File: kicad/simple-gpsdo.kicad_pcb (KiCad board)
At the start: 2 copper layers, 119.5 x 74.5 mm, 90 parts, among them J1 PPS_OUT, J2 PWR, J3 ISP, J6 USB_B_Micro, J7 NEO-6M, J8 10MHz_OUT, Q1 DMP3099L, SW1 RST, U1 BD50FC0FP-E2, U2 ATmega32U4-AU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

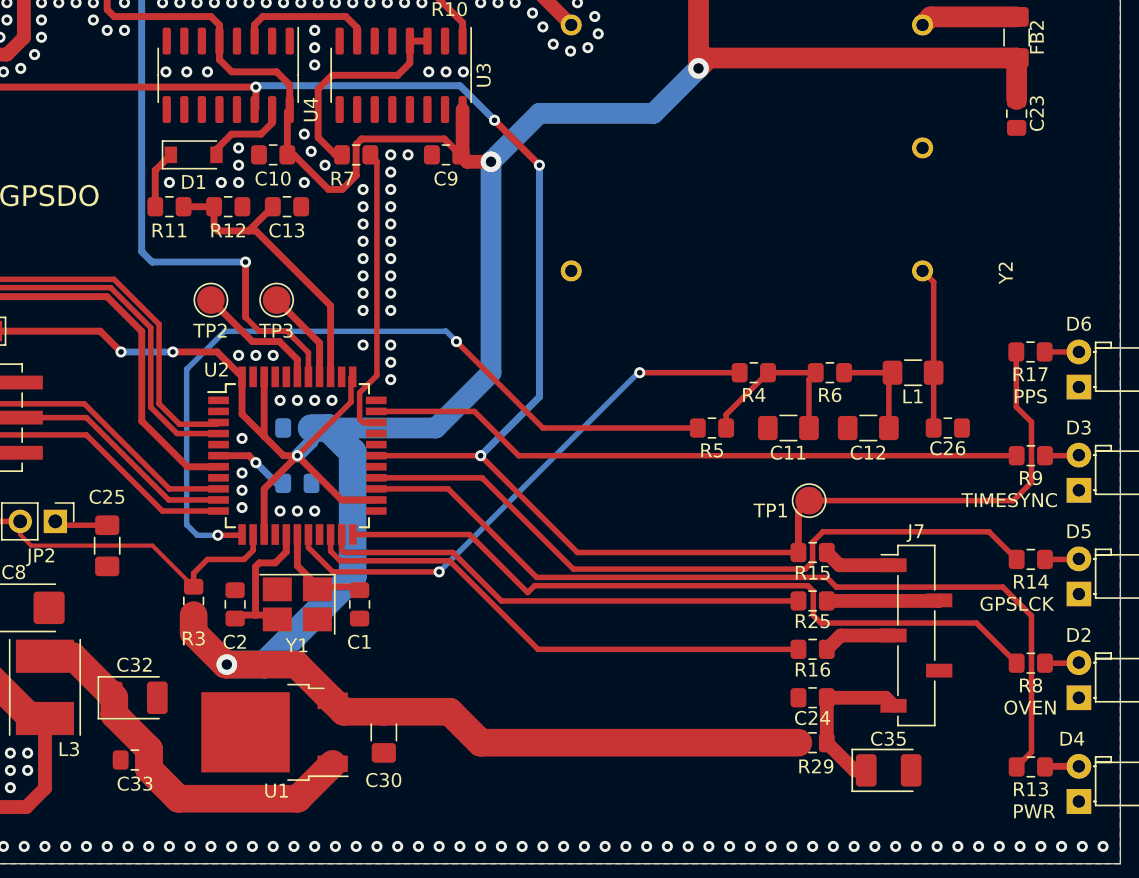
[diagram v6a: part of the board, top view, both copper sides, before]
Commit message: Replaced C23 (0.1uF) with C14 (4.7uF)
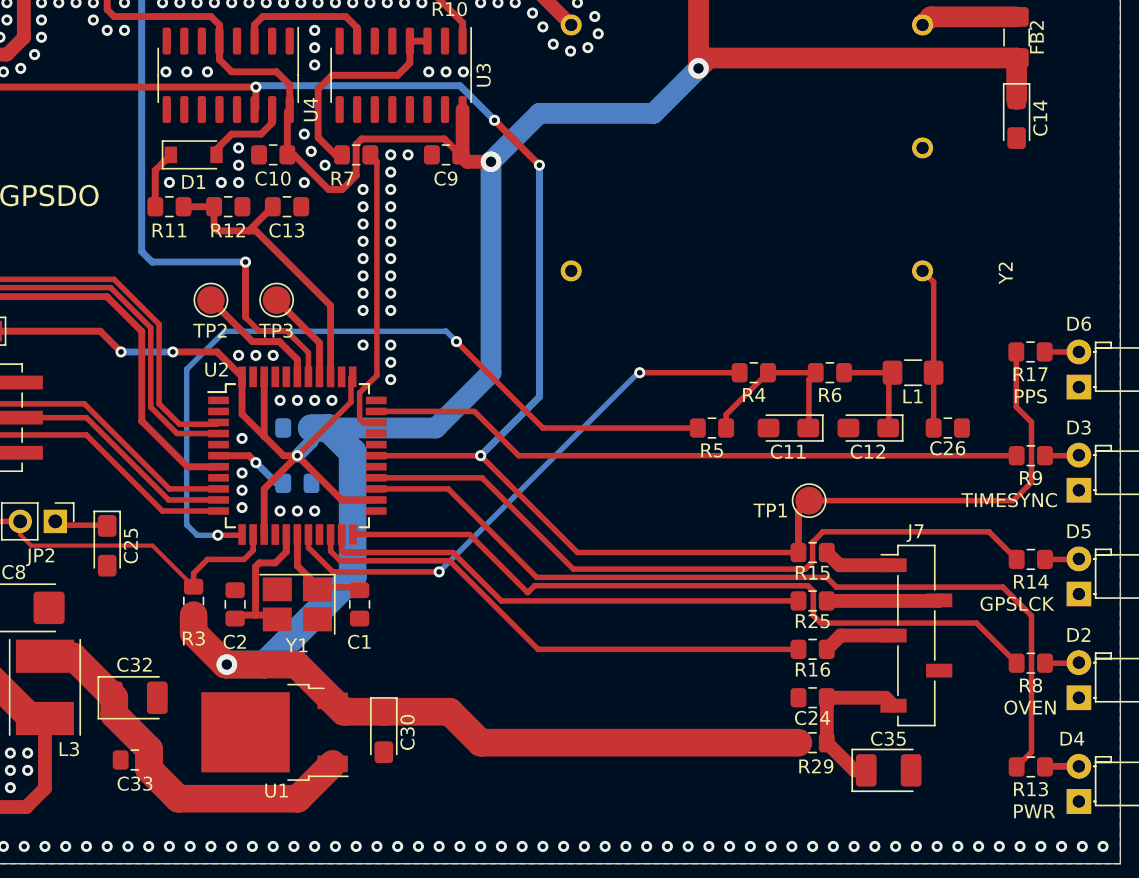
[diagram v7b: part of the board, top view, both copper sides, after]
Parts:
- removed C23: 0.1uF, Capacitor_SMD:C_0805_2012Metric_Pad1.15x1.40mm_HandSolder
- added C14: 4.7uF, Capacitor_Tantalum_SMD:CP_EIA-3216-10_Kemet-I_Pad1.58x1.35mm_HandSolder, F.Cu at (187.0, 95.6)
- C11, C12, C25, C30: footprint Capacitor_SMD:C_1206_3216Metric_Pad1.42x1.75mm_HandSolder -> Capacitor_Tantalum_SMD:CP_EIA-3216-10_Kemet-I_Pad1.58x1.35mm_HandSolder
- D1: value 1N5711 -> 1N6263

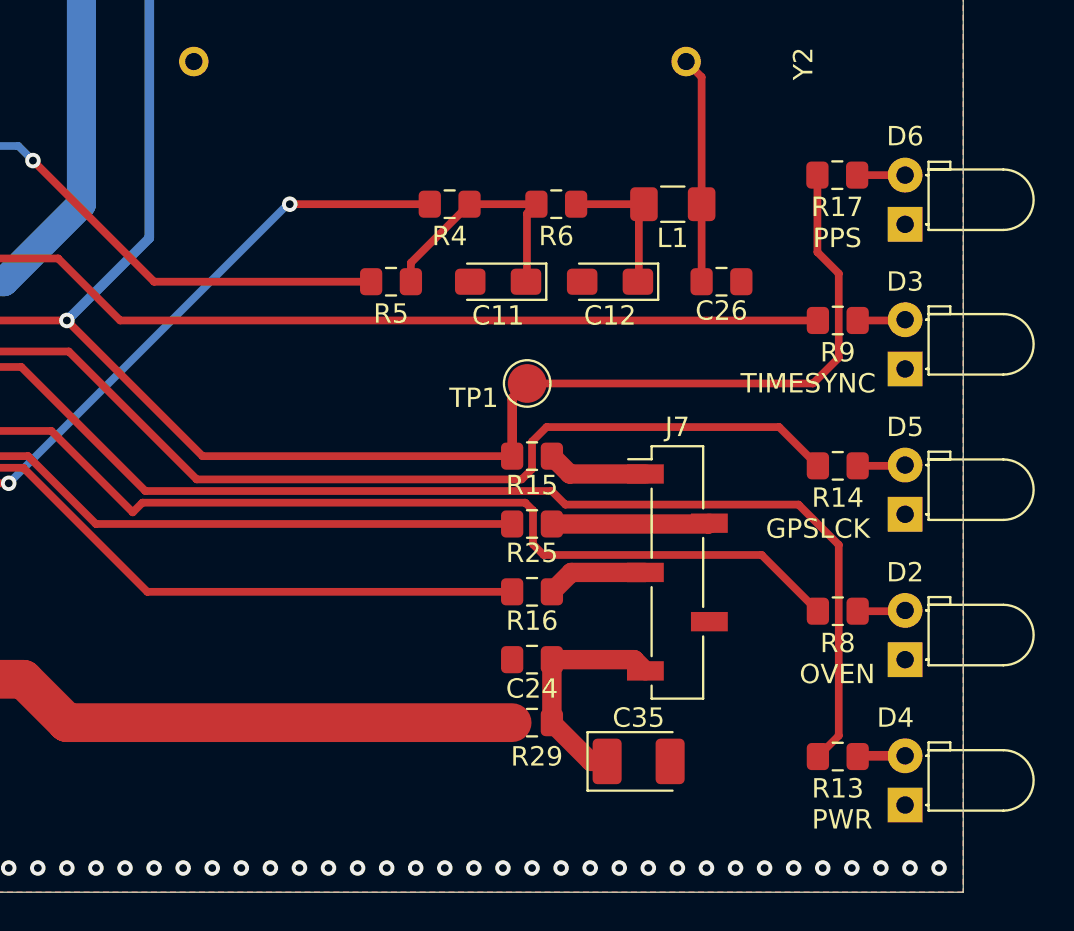
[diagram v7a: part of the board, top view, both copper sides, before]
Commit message: Updated LEDs to proper right angle THT, including 3D models
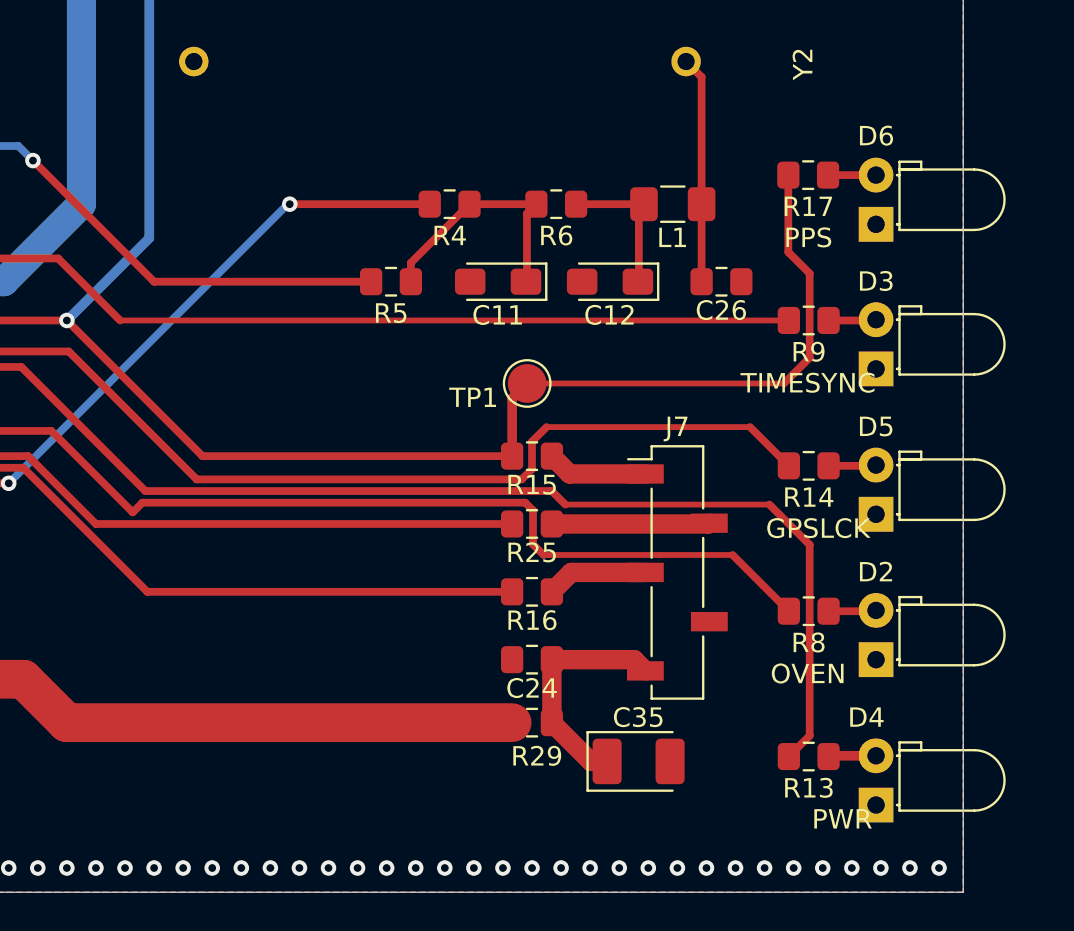
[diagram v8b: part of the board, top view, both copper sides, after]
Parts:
- moved D2 1.50 mm to (190.0, 137.5)
- moved D3 1.50 mm to (190.0, 122.5)
- moved D4 1.50 mm to (190.0, 145.0)
- moved D5 1.50 mm to (190.0, 130.0)
- moved D6 1.50 mm to (190.0, 115.0)
- moved R13 1.50 mm to (186.5, 142.5)
- moved R14 1.50 mm to (186.5, 127.5)
- moved R17 1.50 mm to (186.5, 112.5)
- moved R8 1.50 mm to (186.5, 135.0)
- moved R9 1.50 mm to (186.5, 120.0)
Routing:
- net TIME_LOCK: track 47.6 -> 46.1 mm
- net POWER_OK: track 62.5 -> 61.0 mm
- net OVEN_TEMP: track 53.3 -> 51.8 mm
- net GPS_PPS: track 160.2 -> 158.7 mm
- net GPS_LOCK: track 51.8 -> 50.3 mm
